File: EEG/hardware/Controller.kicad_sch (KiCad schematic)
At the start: 10 parts, among them J5 EXTERNAL_ESP32_3V3, J7 DEV_POWER_LINK

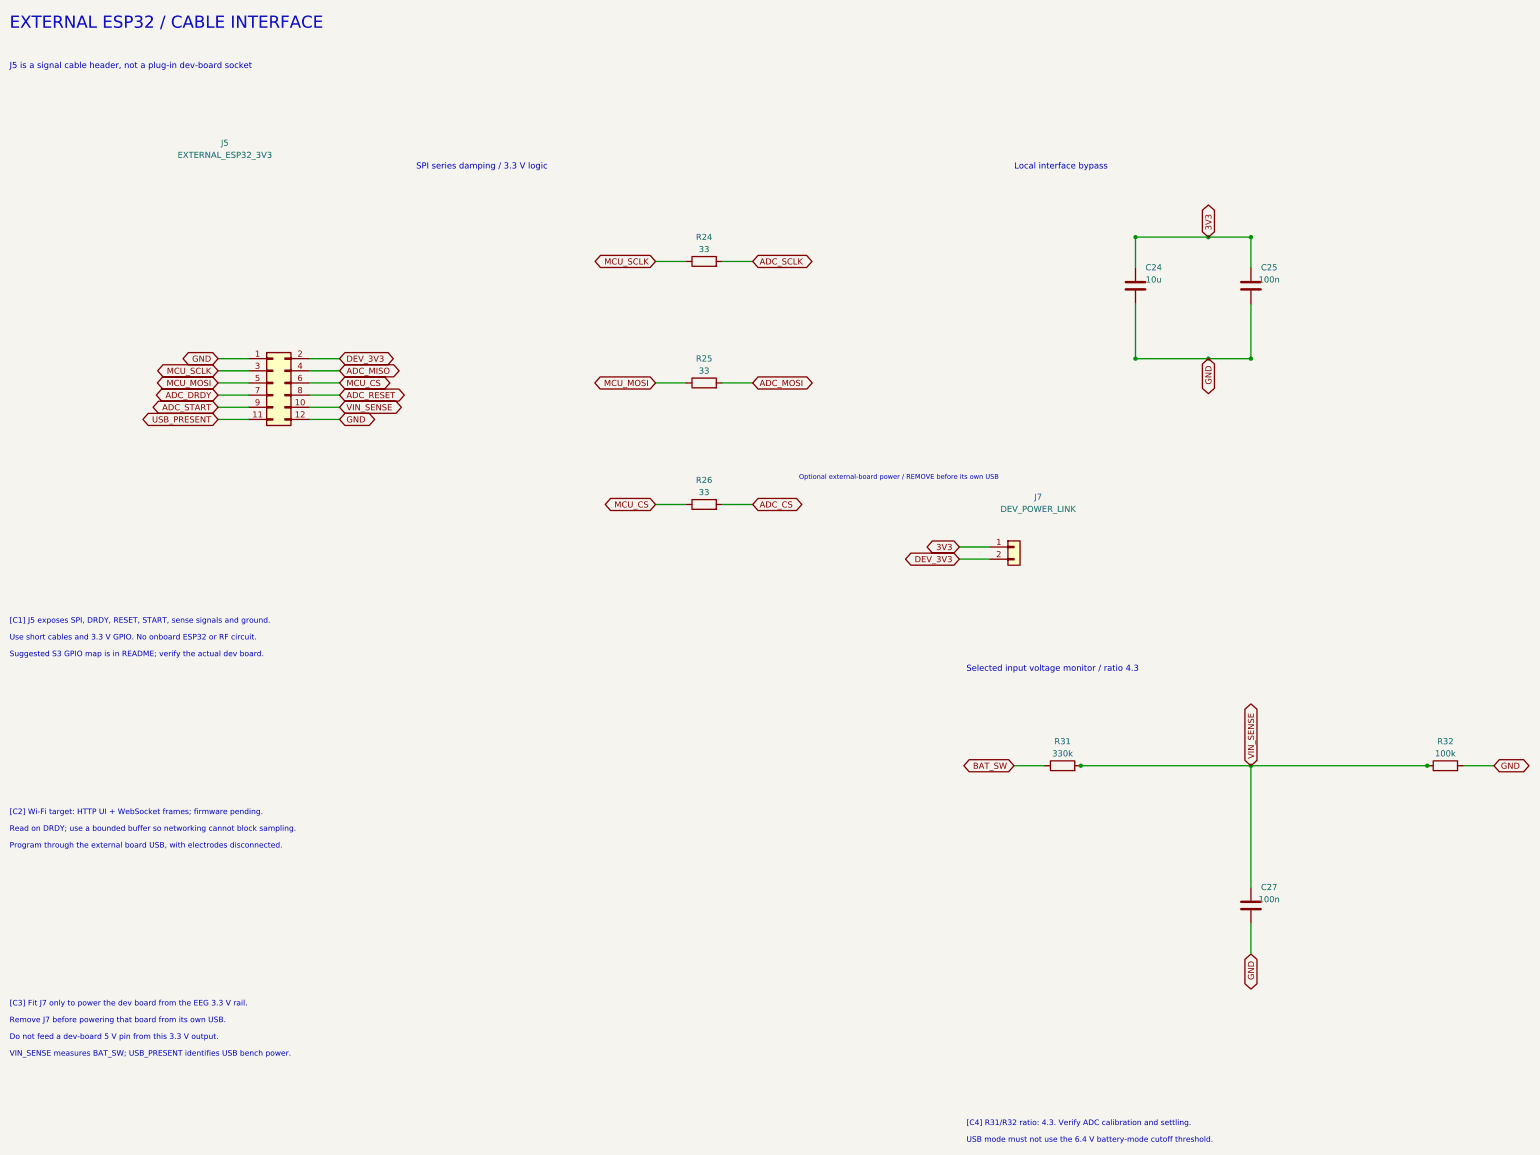
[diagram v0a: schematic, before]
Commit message: feat(eeg): compact and center PCB, add power LED
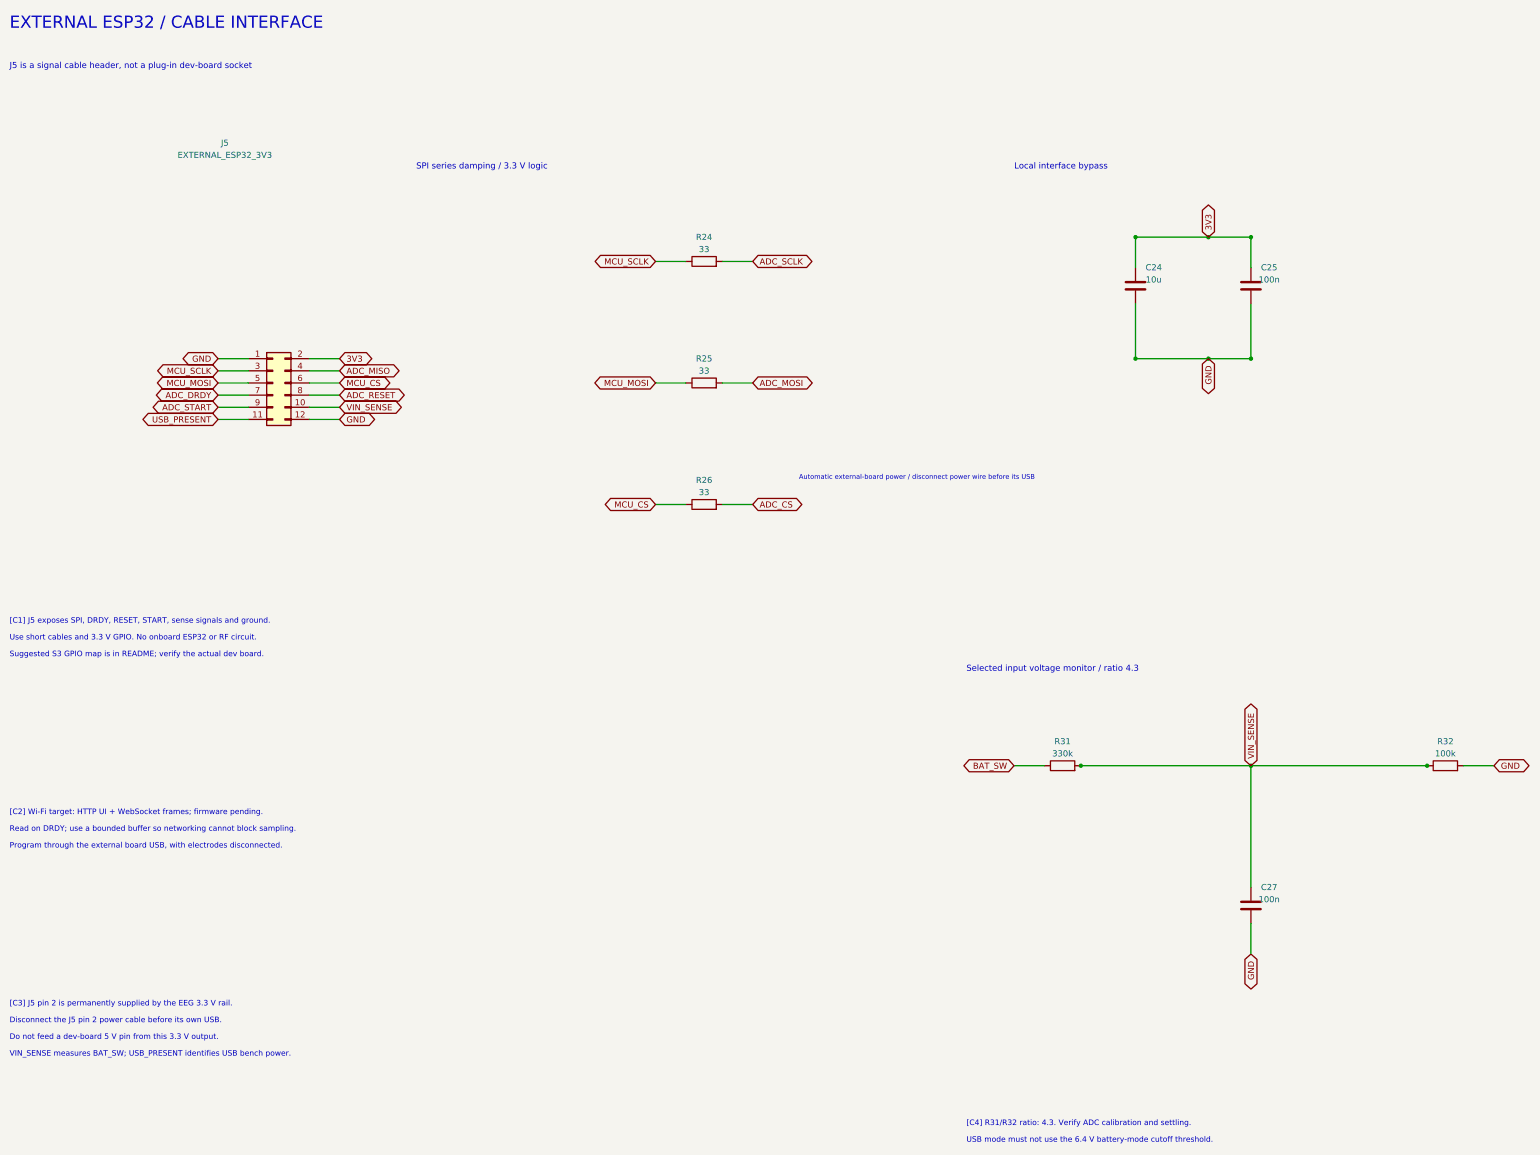
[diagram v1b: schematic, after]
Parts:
- removed J7: DEV_POWER_LINK, Connector_PinHeader_2.54mm:PinHeader_1x02_P2.54mm_Vertical, symbol Connector_Generic:Conn_01x02
- J5: Notes Cable header, NOT a dev-board plug-in socket. 3.3 V logic o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 -> External ESP32 cable; pin 2 permanently powered from 3V3. D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
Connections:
- net DEV_3V3 is gone; now on net 3V3: J5.2 (Pin_2)
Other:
- note added: "Automatic external-board power / disconnect power wire before its USB"
- note added: "Disconnect the J5 pin 2 power cable before its own USB."
- note added: "[C3] J5 pin 2 is permanently supplied by the EEG 3.3 V rail."
- note removed: "Optional external-board power / REMOVE before its own USB"
- note removed: "Remove J7 before powering that board from its own USB."
- note removed: "[C3] Fit J7 only to power the dev board from the EEG 3.3 V rail."
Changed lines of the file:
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@@
       )
     )
-    (property "Notes" "Cable header, NOT a dev-board plug-in socket. 3.3 V logic only."
+    (property "Notes" "External ESP32 cable; pin 2 permanently powered from 3V3. Disconnect its 3V3 cable before powering external board by USB."
       (at 70 52.7 0)
       (effects
@@
     )
   )
-  (symbol
-    (lib_id "Connector_Generic:Conn_01x02")
-    (at 234.95000000000002 124.46000000000001 0)
-    (unit 1)
-    (exclude_from_sim no)
-    (in_bom yes)
-    (on_board yes)
-    (dnp no)
-    (property "Reference" "J7"
-      (at 240 114.0 0)
-      (effects
-        (font
-          (size 1.27 1.27)
-        )
-      )
-    )
-    (property "Value" "DEV_POWER_LINK"
-      (at 240 116.54 0)
-      (effects
-        (font
-          (size 1.27 1.27)
-        )
-      )
-    )
-    (property "Footprint" "Connector_PinHeader_2.54mm:PinHeader_1x02_P2.54mm_Vertical"
-      (at 240 119.08 0)
-      (effects
-        (font
-          (size 1.27 1.27)
-        )
-        (hide yes)
-      )
-    )
-    (property "MPN" "61300211121"
-      (at 240 121.62 0)
-      (effects
-        (font
-          (size 1.27 1.27)
-        )
-        (hide yes)
-      )
-    )
-    (property "Manufacturer" "Wurth Elektronik"
-      (at 240 124.16 0)
-      (effects
-        (font
-          (size 1.27 1.27)
-        )
-        (hide yes)
-      )
-    )
-    (property "Notes" "Fit shunt to power external board through 3V3 pin. Remove before its own USB supply/programming."
-      (at 240 126.7 0)
-      (effects
-        (font
-          (size 1.27 1.27)
-        )
-        (hide yes)
-      )
-    )
-    (instances
-      (project "EEG"
-        (path "/2fc4bea2-122a-5020-9ec0-13f239cb6fbc/59f1ce6a-9eab-50a0-8c46-0fa9b6c7ac44"
-          (reference "J7")
-          (unit 1)
-        )
-      )
-    )
-  )
   (text "EXTERNAL ESP32 / CABLE INTERFACE"
     (at 25 15 0)
@@
     )
   )
-  (text "Optional external-board power / REMOVE before its own USB"
+  (text "Automatic external-board power / disconnect power wire before its USB"
     (at 190 110 0)
     (effects
@@
     )
   )
-  (text "[C3] Fit J7 only to power the dev board from the EEG 3.3 V rail."
+  (text "[C3] J5 pin 2 is permanently supplied by the EEG 3.3 V rail."
     (at 25 220.0 0)
     (effects
@@
     )
   )
-  (text "Remove J7 before powering that board from its own USB."
+  (text "Disconnect the J5 pin 2 power cable before its own USB."
     (at 25 223.5 0)
     (effects
@@
     )
   )
-  (global_label "DEV_3V3"
+  (global_label "3V3"
     (shape bidirectional)
     (at 93.98 85.09 0.0)
@@
     )
   )
-  (wire
-    (pts
-      (xy 229.87 124.46)
-      (xy 223.52 124.46)
-    )
-    (stroke
-      (width 0)
-      (type default)
-    )
-  )
-  (global_label "3V3"
-    (shape bidirectional)
-    (at 223.52 124.46 180.0)
-    (effects
-      (font
-        (size 1.27 1.27)
-      )
-      (justify right)
-    )
-  )
-  (wire
-    (pts
-      (xy 229.87 127.0)
-      (xy 223.52 127.0)
-    )
-    (stroke
-      (width 0)
-      (type default)
-    )
-  )
-  (global_label "DEV_3V3"
-    (shape bidirectional)
-    (at 223.52 127.0 180.0)
-    (effects
-      (font
-        (size 1.27 1.27)
-      )
-      (justify right)
-    )
-  )
